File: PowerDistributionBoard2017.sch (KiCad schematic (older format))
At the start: 1 part

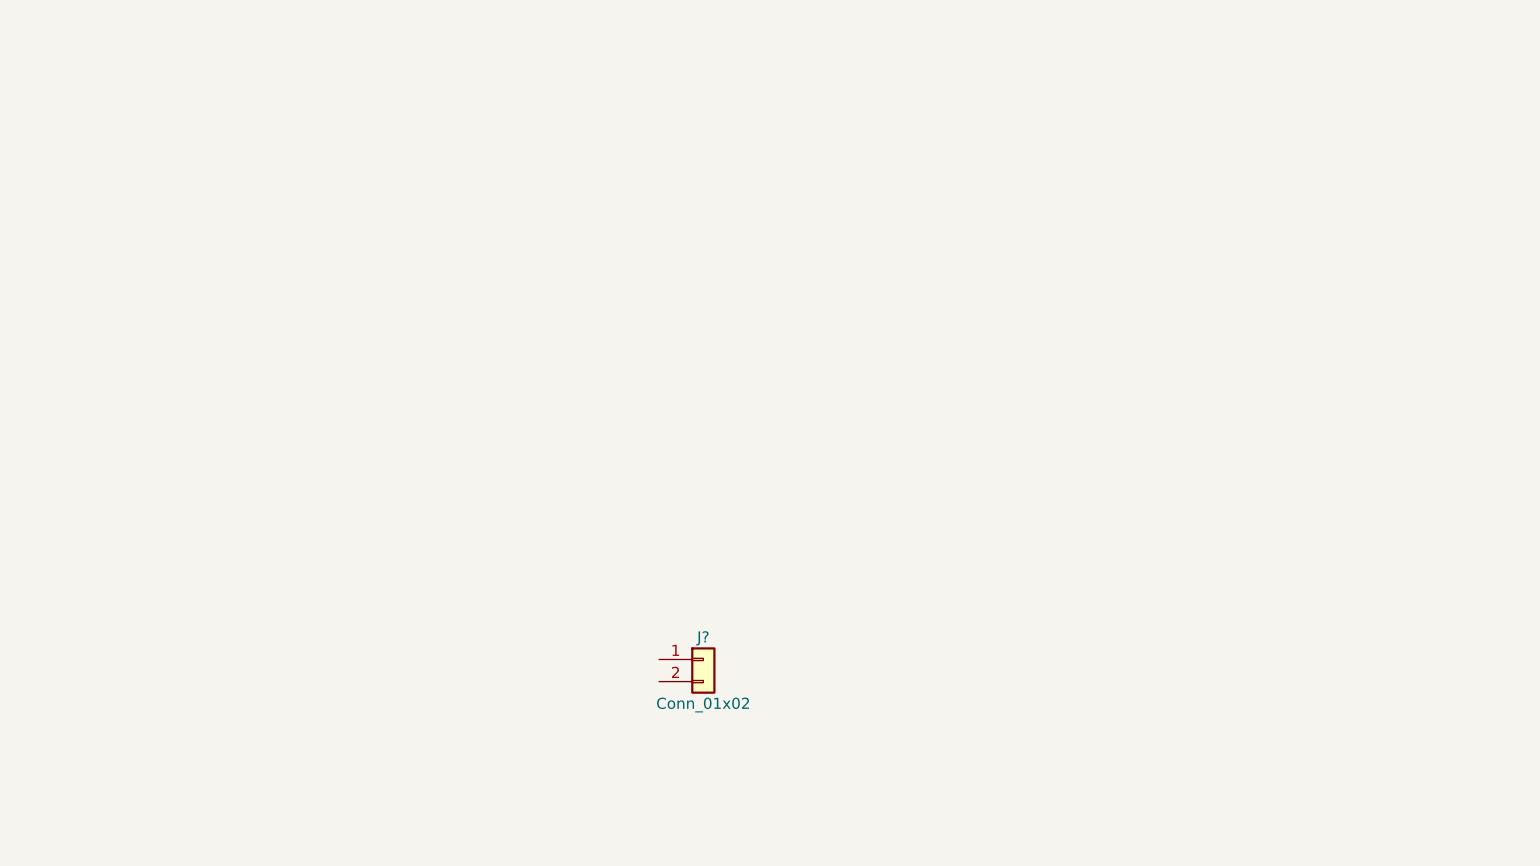
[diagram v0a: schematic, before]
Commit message: I added all of the components to EBM and JM. Hopefully that finishes up the schematic! Let me know if something needs to be changed/ added.
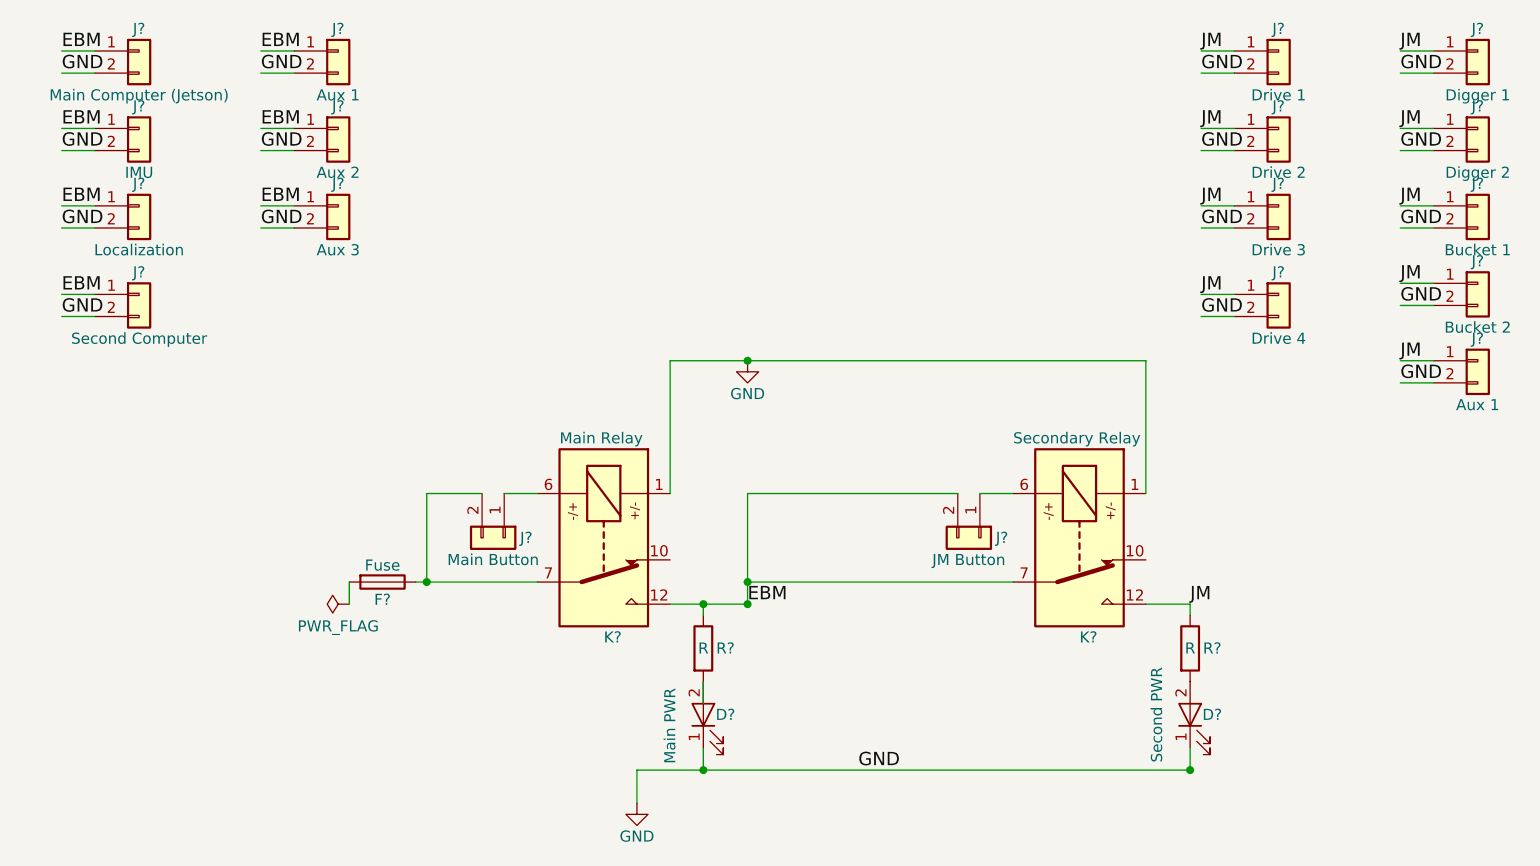
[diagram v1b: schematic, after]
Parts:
- added D?: Main PWR, symbol LED
- added D?: Second PWR, symbol LED
- added F?: Fuse, symbol Fuse
- added J?: JM Button, symbol Conn_01x02
- added J?: Main Computer (Jetson), symbol Conn_01x02
- added J?: Second Computer, symbol Conn_01x02
- added J?: IMU, symbol Conn_01x02
- added J?: Localization, symbol Conn_01x02
- added J? (x2): Aux 1, symbol Conn_01x02
- added J?: Aux 2, symbol Conn_01x02
- added J?: Aux 3, symbol Conn_01x02
- added J?: Drive 1, symbol Conn_01x02
- added J?: Drive 4, symbol Conn_01x02
- added J?: Drive 2, symbol Conn_01x02
- added J?: Drive 3, symbol Conn_01x02
- added J?: Digger 1, symbol Conn_01x02
- added J?: Digger 2, symbol Conn_01x02
- added J?: Bucket 1, symbol Conn_01x02
- added J?: Bucket 2, symbol Conn_01x02
- added K?: Main Relay, Relays_THT:Relay_SPDT_OMRON-G6E, symbol G6EU
- added K?: Secondary Relay, Relays_THT:Relay_SPDT_OMRON-G6E, symbol G6EU
- added R? (x2): R, symbol R
- J?: value Conn_01x02 -> Main Button
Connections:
- net at J?.1 (Pin_1): now also K?.6
- net at J?.2 (Pin_2): now also F?.1, K?.7
- new net: J?.1 (Pin_1), K?.6
- new net: D?.2 (A), R?.2 (x2)
- new net EBM: J?.1 (Pin_1), J?.1 (Pin_1), J?.1 (Pin_1), J?.1 (Pin_1), J?.1 (Pin_1), J?.1 (Pin_1), J?.1 (Pin_1), J?.2 (Pin_2), K?.12, K?.7, R?.1
- new net GND: D?.1 (K), D?.1 (K), J?.2 (Pin_2), J?.2 (Pin_2), J?.2 (Pin_2), J?.2 (Pin_2), J?.2 (Pin_2), J?.2 (Pin_2), J?.2 (Pin_2), J?.2 (Pin_2), J?.2 (Pin_2), J?.2 (Pin_2), J?.2 (Pin_2), J?.2 (Pin_2), J?.2 (Pin_2), J?.2 (Pin_2), J?.2 (Pin_2), J?.2 (Pin_2), K?.1, K?.1
- new net JM: J?.1 (Pin_1), J?.1 (Pin_1), J?.1 (Pin_1), J?.1 (Pin_1), J?.1 (Pin_1), J?.1 (Pin_1), J?.1 (Pin_1), J?.1 (Pin_1), J?.1 (Pin_1), K?.12, R?.1
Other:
- moved on the sheet: J?

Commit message: Added annotations, electrical check. Few issues, unresolved.
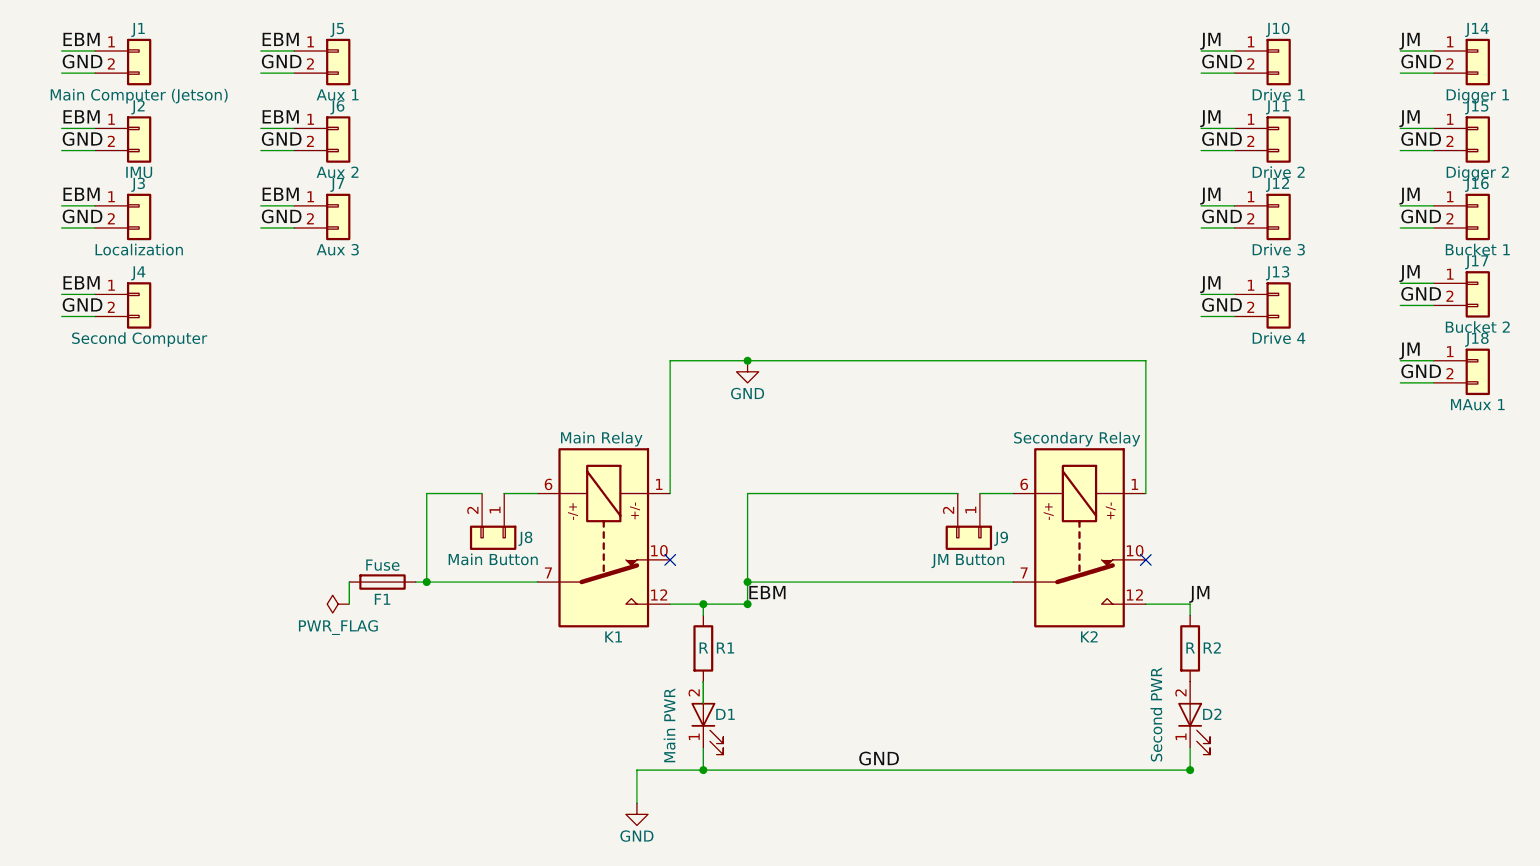
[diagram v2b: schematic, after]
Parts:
- J18: renamed from J?; value Aux 1 -> MAux 1
- gave numbers to parts that had none: 24
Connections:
- no-connect marks 0 -> 2
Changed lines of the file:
@@
 $EndDescr
 $Comp
-L Conn_01x02 J?
+L Conn_01x02 J8
 U 1 1 59ECFE2F
 P 4400 3150
-F 0 "J?" V 4400 3250 50  0000 C CNN
+F 0 "J8" V 4400 3250 50  0000 C CNN
 F 1 "Main Button" V 4500 3100 50  0000 C CNN
 F 2 "" H 4400 3150 50  0001 C CNN
@@
 $EndComp
 $Comp
-L Fuse F?
+L Fuse F1
 U 1 1 59F39A48
 P 3850 3350
-F 0 "F?" V 3930 3350 50  0000 C CNN
+F 0 "F1" V 3930 3350 50  0000 C CNN
 F 1 "Fuse" V 3775 3350 50  0000 C CNN
 F 2 "" V 3780 3350 50  0001 C CNN
@@
 $EndComp
 $Comp
-L G6EU K?
+L G6EU K1
 U 1 1 59F39B7C
 P 4850 3150
-F 0 "K?" V 5300 3150 50  0000 L CNN
+F 0 "K1" V 5300 3150 50  0000 L CNN
 F 1 "Main Relay" V 4400 2950 50  0000 L CNN
 F 2 "Relays_THT:Relay_SPDT_OMRON-G6E" H 5980 3120 50  0001 C CNN
@@
 $EndComp
 $Comp
-L G6EU K?
+L G6EU K2
 U 1 1 59F39D37
 P 7000 3150
-F 0 "K?" V 7450 3150 50  0000 L CNN
+F 0 "K2" V 7450 3150 50  0000 L CNN
 F 1 "Secondary Relay" V 6550 2850 50  0000 L CNN
 F 2 "Relays_THT:Relay_SPDT_OMRON-G6E" H 8130 3120 50  0001 C CNN
@@
 $EndComp
 $Comp
-L R R?
+L R R1
 U 1 1 59F39E5B
 P 5300 3650
-F 0 "R?" H 5400 3650 50  0000 C CNN
+F 0 "R1" H 5400 3650 50  0000 C CNN
 F 1 "R" H 5300 3650 50  0000 C CNN
 F 2 "" V 5230 3650 50  0001 C CNN
@@
 $EndComp
 $Comp
-L R R?
+L R R2
 U 1 1 59F3A0CC
 P 7500 3650
-F 0 "R?" H 7600 3650 50  0000 C CNN
+F 0 "R2" H 7600 3650 50  0000 C CNN
 F 1 "R" H 7500 3650 50  0000 C CNN
 F 2 "" V 7430 3650 50  0001 C CNN
@@
 $EndComp
 $Comp
-L LED D?
+L LED D1
 U 1 1 59F3A324
 P 5300 3950
-F 0 "D?" V 5300 3850 50  0000 C CNN
+F 0 "D1" V 5300 3850 50  0000 C CNN
 F 1 "Main PWR" H 5250 4100 50  0000 C CNN
 F 2 "" H 5300 3950 50  0001 C CNN
@@
 $EndComp
 $Comp
-L LED D?
+L LED D2
 U 1 1 59F3A385
 P 7500 3950
-F 0 "D?" V 7500 3850 50  0000 C CNN
+F 0 "D2" V 7500 3850 50  0000 C CNN
 F 1 "Second PWR" H 7500 4100 50  0000 C CNN
 F 2 "" H 7500 3950 50  0001 C CNN
@@
 	4400 2950 4550 2950
 $Comp
-L Conn_01x02 J?
+L Conn_01x02 J9
 U 1 1 59F3B39B
 P 6550 3150
-F 0 "J?" V 6550 3250 50  0000 C CNN
+F 0 "J9" V 6550 3250 50  0000 C CNN
 F 1 "JM Button" V 6650 3100 50  0000 C CNN
 F 2 "" H 6550 3150 50  0001 C CNN
@@
 GND
 $Comp
-L Conn_01x02 J?
+L Conn_01x02 J1
 U 1 1 59F3DD72
 P 2750 950
-F 0 "J?" H 2750 1050 50  0000 C CNN
+F 0 "J1" H 2750 1050 50  0000 C CNN
 F 1 "Main Computer (Jetson)" H 2750 750 50  0000 C CNN
 F 2 "" H 2750 950 50  0001 C CNN
@@
 GND
 $Comp
-L Conn_01x02 J?
+L Conn_01x02 J4
 U 1 1 59F3DEBC
 P 2750 2050
-F 0 "J?" H 2750 2150 50  0000 C CNN
+F 0 "J4" H 2750 2150 50  0000 C CNN
 F 1 "Second Computer" H 2750 1850 50  0000 C CNN
 F 2 "" H 2750 2050 50  0001 C CNN
@@
 GND
 $Comp
-L Conn_01x02 J?
+L Conn_01x02 J2
 U 1 1 59F3DF19
 P 2750 1300
-F 0 "J?" H 2750 1400 50  0000 C CNN
+F 0 "J2" H 2750 1400 50  0000 C CNN
 F 1 "IMU" H 2750 1100 50  0000 C CNN
 F 2 "" H 2750 1300 50  0001 C CNN
@@
 GND
 $Comp
-L Conn_01x02 J?
+L Conn_01x02 J3
 U 1 1 59F7D9B4
 P 2750 1650
-F 0 "J?" H 2750 1750 50  0000 C CNN
+F 0 "J3" H 2750 1750 50  0000 C CNN
 F 1 "Localization" H 2750 1450 50  0000 C CNN
 F 2 "" H 2750 1650 50  0001 C CNN
@@
 GND
 $Comp
-L Conn_01x02 J?
+L Conn_01x02 J5
 U 1 1 59F7DE49
 P 3650 950
-F 0 "J?" H 3650 1050 50  0000 C CNN
+F 0 "J5" H 3650 1050 50  0000 C CNN
 F 1 "Aux 1" H 3650 750 50  0000 C CNN
 F 2 "" H 3650 950 50  0001 C CNN
@@
 GND
 $Comp
-L Conn_01x02 J?
+L Conn_01x02 J6
 U 1 1 59F7DE5D
 P 3650 1300
-F 0 "J?" H 3650 1400 50  0000 C CNN
+F 0 "J6" H 3650 1400 50  0000 C CNN
 F 1 "Aux 2" H 3650 1100 50  0000 C CNN
 F 2 "" H 3650 1300 50  0001 C CNN
@@
 GND
 $Comp
-L Conn_01x02 J?
+L Conn_01x02 J7
 U 1 1 59F7DE67
 P 3650 1650
-F 0 "J?" H 3650 1750 50  0000 C CNN
+F 0 "J7" H 3650 1750 50  0000 C CNN
 F 1 "Aux 3" H 3650 1450 50  0000 C CNN
 F 2 "" H 3650 1650 50  0001 C CNN
@@
 GND
 $Comp
-L Conn_01x02 J?
+L Conn_01x02 J10
 U 1 1 59F7EA88
 P 7900 950
-F 0 "J?" H 7900 1050 50  0000 C CNN
+F 0 "J10" H 7900 1050 50  0000 C CNN
 F 1 "Drive 1" H 7900 750 50  0000 C CNN
 F 2 "" H 7900 950 50  0001 C CNN
@@
 GND
 $Comp
-L Conn_01x02 J?
+L Conn_01x02 J13
 U 1 1 59F7EA92
 P 7900 2050
-F 0 "J?" H 7900 2150 50  0000 C CNN
+F 0 "J13" H 7900 2150 50  0000 C CNN
 F 1 "Drive 4" H 7900 1850 50  0000 C CNN
 F 2 "" H 7900 2050 50  0001 C CNN
@@
 GND
 $Comp
-L Conn_01x02 J?
+L Conn_01x02 J11
 U 1 1 59F7EA9C
 P 7900 1300
-F 0 "J?" H 7900 1400 50  0000 C CNN
+F 0 "J11" H 7900 1400 50  0000 C CNN
 F 1 "Drive 2" H 7900 1100 50  0000 C CNN
 F 2 "" H 7900 1300 50  0001 C CNN
@@
 GND
 $Comp
-L Conn_01x02 J?
+L Conn_01x02 J12
 U 1 1 59F7EAA6
 P 7900 1650
-F 0 "J?" H 7900 1750 50  0000 C CNN
+F 0 "J12" H 7900 1750 50  0000 C CNN
 F 1 "Drive 3" H 7900 1450 50  0000 C CNN
 F 2 "" H 7900 1650 50  0001 C CNN
@@
 GND
 $Comp
-L Conn_01x02 J?
+L Conn_01x02 J14
 U 1 1 59F7EAB0
 P 8800 950
-F 0 "J?" H 8800 1050 50  0000 C CNN
+F 0 "J14" H 8800 1050 50  0000 C CNN
 F 1 "Digger 1" H 8800 750 50  0000 C CNN
 F 2 "" H 8800 950 50  0001 C CNN
@@
 GND
 $Comp
-L Conn_01x02 J?
+L Conn_01x02 J15
 U 1 1 59F7EABA
 P 8800 1300
-F 0 "J?" H 8800 1400 50  0000 C CNN
+F 0 "J15" H 8800 1400 50  0000 C CNN
 F 1 "Digger 2" H 8800 1100 50  0000 C CNN
 F 2 "" H 8800 1300 50  0001 C CNN
@@
 GND
 $Comp
-L Conn_01x02 J?
+L Conn_01x02 J16
 U 1 1 59F7EAC4
 P 8800 1650
-F 0 "J?" H 8800 1750 50  0000 C CNN
+F 0 "J16" H 8800 1750 50  0000 C CNN
 F 1 "Bucket 1" H 8800 1450 50  0000 C CNN
 F 2 "" H 8800 1650 50  0001 C CNN
@@
 GND
 $Comp
-L Conn_01x02 J?
+L Conn_01x02 J17
 U 1 1 59F7EB2A
 P 8800 2000
-F 0 "J?" H 8800 2100 50  0000 C CNN
+F 0 "J17" H 8800 2100 50  0000 C CNN
 F 1 "Bucket 2" H 8800 1800 50  0000 C CNN
 F 2 "" H 8800 2000 50  0001 C CNN
@@
 GND
 $Comp
-L Conn_01x02 J?
+L Conn_01x02 J18
 U 1 1 59F7EB34
 P 8800 2350
-F 0 "J?" H 8800 2450 50  0000 C CNN
-F 1 "Aux 1" H 8800 2150 50  0000 C CNN
+F 0 "J18" H 8800 2450 50  0000 C CNN
+F 1 "MAux 1" H 8800 2150 50  0000 C CNN
 F 2 "" H 8800 2350 50  0001 C CNN
 F 3 "" H 8800 2350 50  0001 C CNN
@@
 Text Label 8450 2450 0    60   ~ 0
 GND
+NoConn ~ 5150 3250
+NoConn ~ 7300 3250
 $EndSCHEMATC
